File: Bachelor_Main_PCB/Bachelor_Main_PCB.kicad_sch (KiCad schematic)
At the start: 4 parts

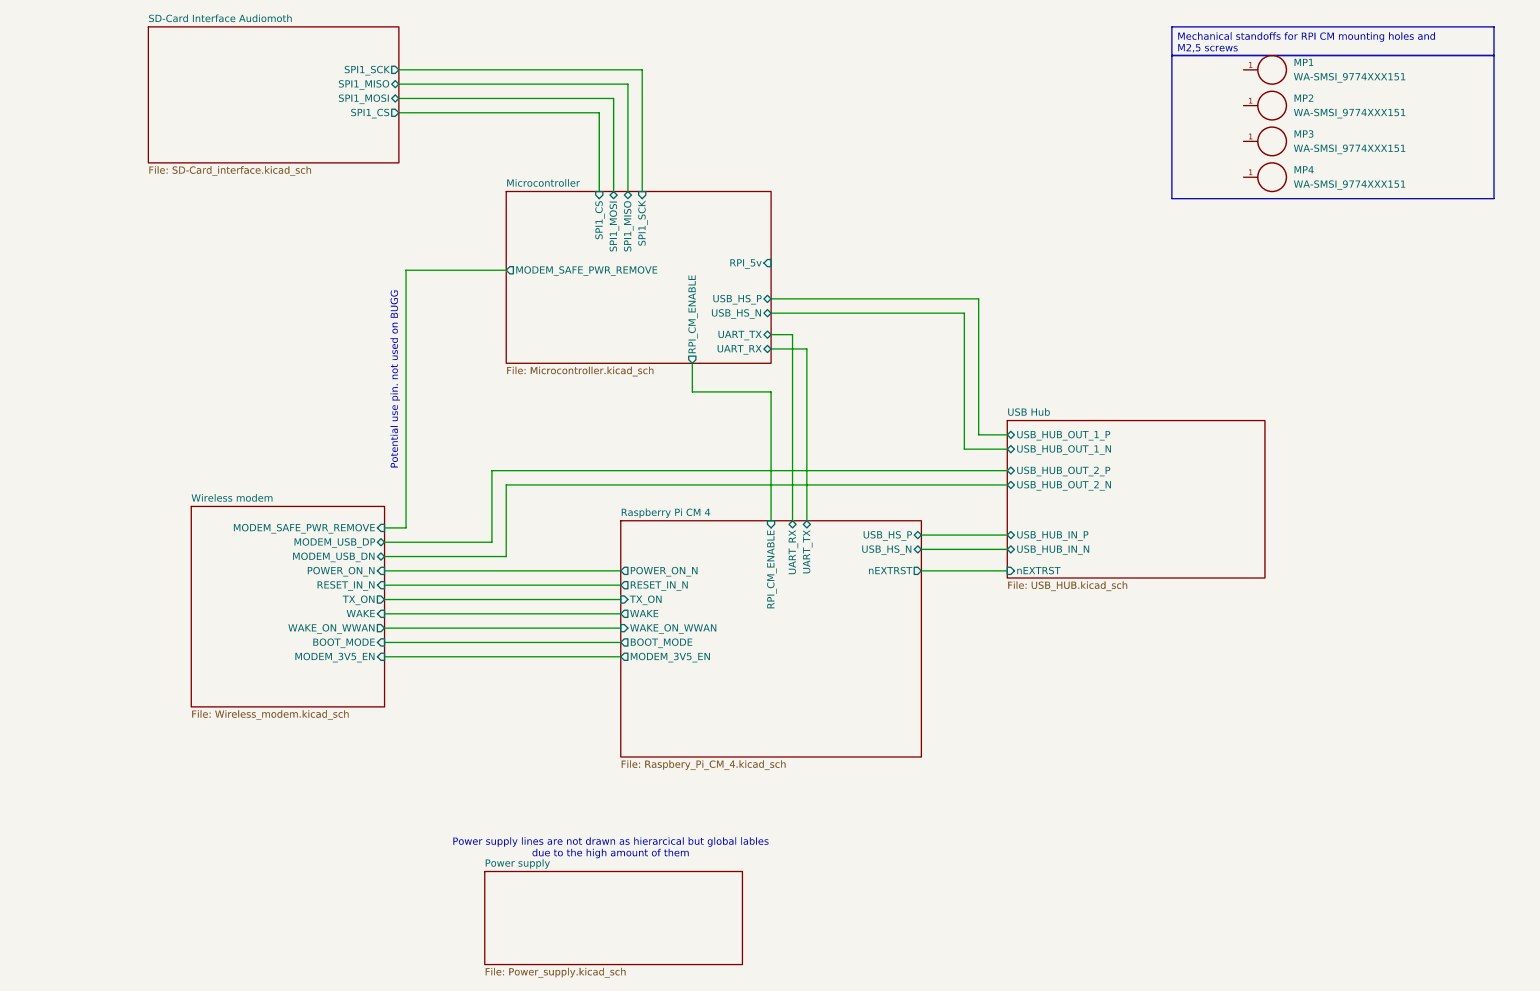
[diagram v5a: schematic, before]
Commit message: Add Vin sampling and route V_IN and V_IMON to MCU sheet
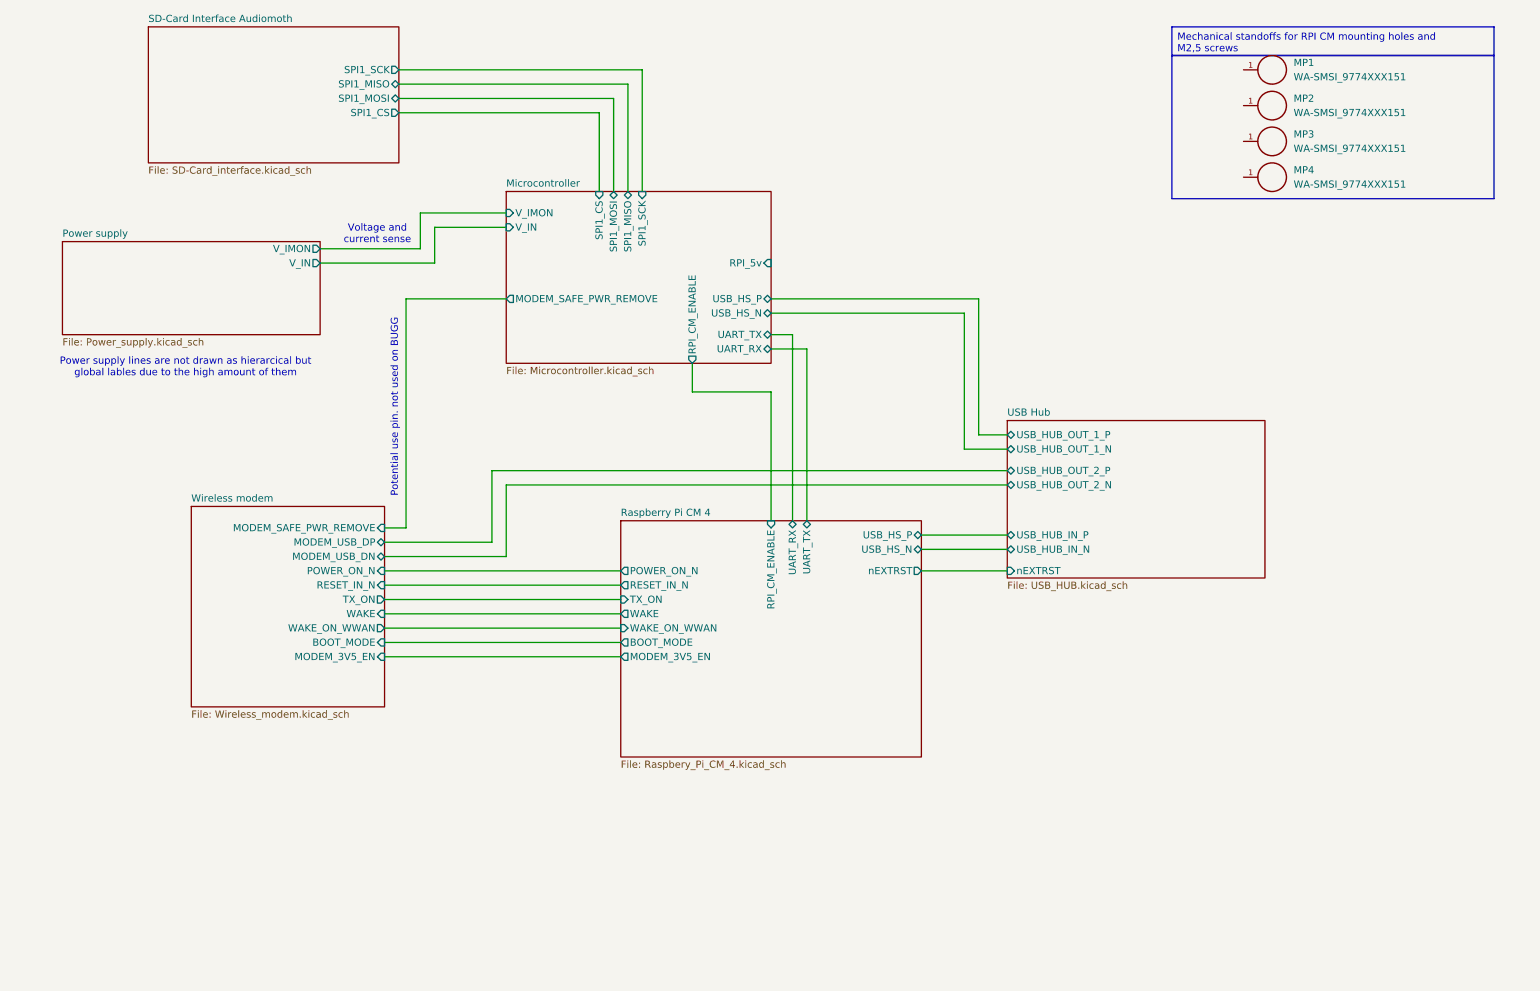
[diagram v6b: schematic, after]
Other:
- sheet Microcontroller ports: added V_IMON, V_IN; removed none
- sheet Power supply ports: added V_IMON, V_IN; removed none
- note added: "Voltage and current sense"
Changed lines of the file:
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@@
 	(generator_version "9.0")
 	(paper "A4")
-	(text "Power supply lines are not drawn as hierarcical but global lables\ndue to the high amount of them"
+	(text "Voltage and \ncurrent sense"
 		(exclude_from_sim no)
-		(at 120.142 163.576 0)
+		(at 78.74 54.61 0)
 		(effects
 			(font
@@
 		)
 	)
+	(text "Power supply lines are not drawn as hierarcical but \nglobal lables due to the high amount of them"
+		(exclude_from_sim no)
+		(at 44.704 78.232 0)
+		(effects
+			(font
+				(size 1.27 1.27)
+			)
+		)
+	)
 	(text "Potential use pin. not used on BUGG"
 		(exclude_from_sim no)
-		(at 81.788 80.518 90)
+		(at 81.788 85.344 90)
 		(effects
 			(font
@@
 	(wire
 		(pts
+			(xy 86.36 57.15) (xy 86.36 50.8)
+		)
+		(stroke
+			(width 0)
+			(type default)
+		)
+	)
+	(wire
+		(pts
 			(xy 120.65 30.48) (xy 82.55 30.48)
 		)
@@
 	(wire
 		(pts
-			(xy 83.82 60.96) (xy 101.6 60.96)
+			(xy 83.82 66.04) (xy 101.6 66.04)
 		)
 		(stroke
@@
 	(wire
 		(pts
+			(xy 101.6 53.34) (xy 88.9 53.34)
+		)
+		(stroke
+			(width 0)
+			(type default)
+		)
+	)
+	(wire
+		(pts
 			(xy 148.59 105.41) (xy 148.59 82.55)
 		)
@@
 	(wire
 		(pts
+			(xy 86.36 50.8) (xy 101.6 50.8)
+		)
+		(stroke
+			(width 0)
+			(type default)
+		)
+	)
+	(wire
+		(pts
+			(xy 88.9 59.69) (xy 68.58 59.69)
+		)
+		(stroke
+			(width 0)
+			(type default)
+		)
+	)
+	(wire
+		(pts
 			(xy 80.01 124.46) (xy 121.92 124.46)
 		)
@@
 	(wire
 		(pts
-			(xy 83.82 106.68) (xy 83.82 60.96)
+			(xy 83.82 106.68) (xy 83.82 66.04)
 		)
 		(stroke
@@
 	(wire
 		(pts
+			(xy 88.9 53.34) (xy 88.9 59.69)
+		)
+		(stroke
+			(width 0)
+			(type default)
+		)
+	)
+	(wire
+		(pts
 			(xy 134.62 82.55) (xy 134.62 77.47)
 		)
@@
 		(pts
 			(xy 80.01 119.38) (xy 121.92 119.38)
+		)
+		(stroke
+			(width 0)
+			(type default)
+		)
+	)
+	(wire
+		(pts
+			(xy 68.58 57.15) (xy 86.36 57.15)
 		)
 		(stroke
@@
 	)
 	(sheet
-		(at 97.79 167.64)
+		(at 22.86 55.88)
 		(size 45.72 16.51)
 		(exclude_from_sim no)
@@
 		)
 		(property "Sheetname" "Power supply"
-			(at 97.79 166.9284 0)
+			(at 22.86 55.1684 0)
 			(effects
 				(font
@@
 		)
 		(property "Sheetfile" "Power_supply.kicad_sch"
-			(at 97.79 184.7346 0)
+			(at 22.86 72.9746 0)
 			(effects
 				(font
@@
 				)
 				(justify left top)
+			)
+		)
+		(pin "V_IMON" output
+			(at 68.58 57.15 0)
+			(effects
+				(font
+					(size 1.27 1.27)
+				)
+				(justify right)
+			)
+		)
+		(pin "V_IN" output
+			(at 68.58 59.69 0)
+			(effects
+				(font
+					(size 1.27 1.27)
+				)
+				(justify right)
 			)
 		)
@@
 		)
 		(pin "MODEM_SAFE_PWR_REMOVE" output
-			(at 101.6 60.96 180)
+			(at 101.6 66.04 180)
 			(effects
 				(font
@@
 			)
 		)
+		(pin "V_IMON" input
+			(at 101.6 50.8 180)
+			(effects
+				(font
+					(size 1.27 1.27)
+				)
+				(justify left)
+			)
+		)
+		(pin "V_IN" input
+			(at 101.6 53.34 180)
+			(effects
+				(font
+					(size 1.27 1.27)
+				)
+				(justify left)
+			)
+		)

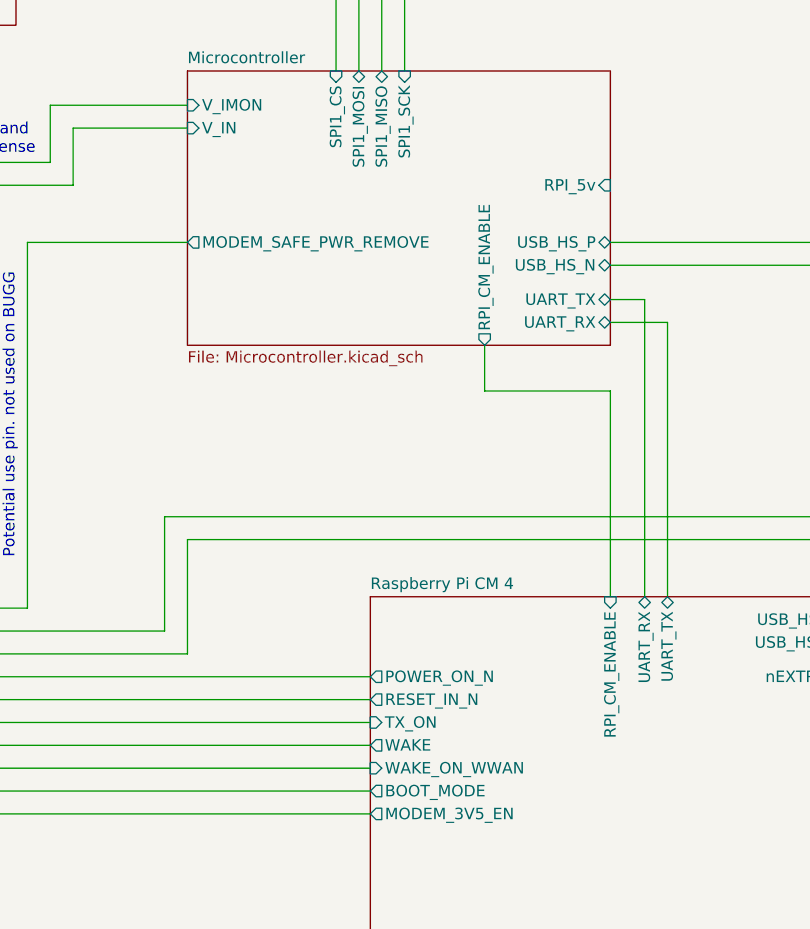
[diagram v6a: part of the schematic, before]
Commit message: Remove RPI CM power on mosfet. Replaced with EN pin to PSU
the pin is now routed instead to the LMR51450 converter ENABLE pin.
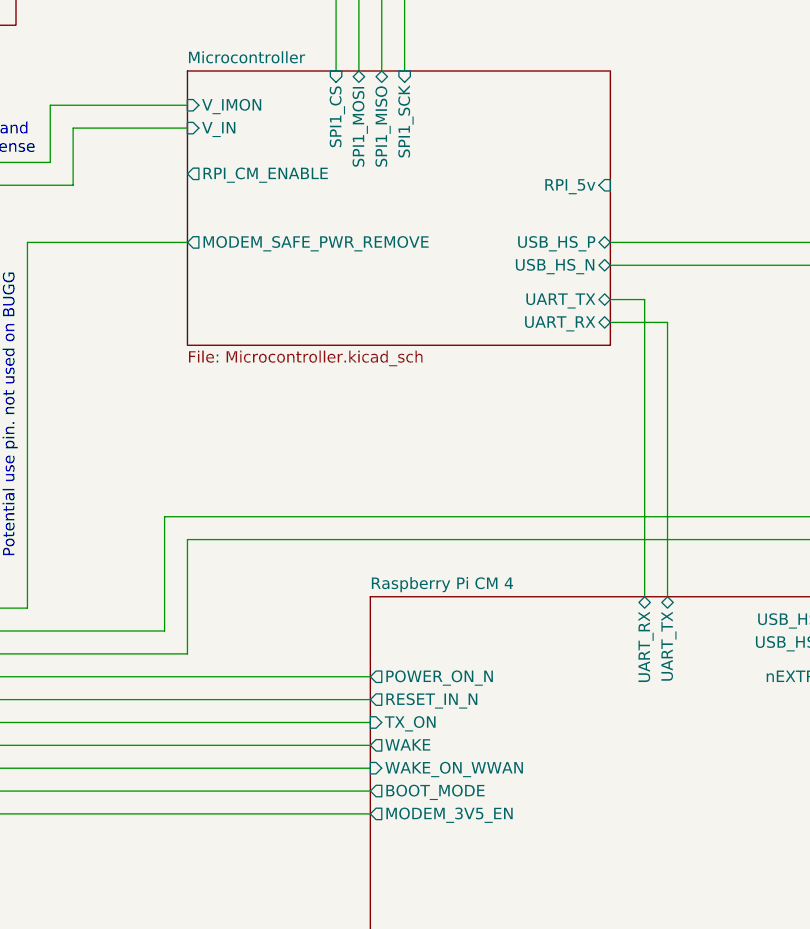
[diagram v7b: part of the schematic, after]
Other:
- sheet Raspberry Pi CM 4 ports: added none; removed RPI_CM_ENABLE
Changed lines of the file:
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@@
-	(wire
-		(pts
-			(xy 148.59 105.41) (xy 148.59 82.55)
-		)
-		(stroke
-			(width 0)
-			(type default)
-		)
-	)
 	(wire
 		(pts
@@
 	(wire
 		(pts
-			(xy 148.59 82.55) (xy 134.62 82.55)
-		)
-		(stroke
-			(width 0)
-			(type default)
-		)
-	)
-	(wire
-		(pts
 			(xy 88.9 53.34) (xy 88.9 59.69)
-		)
-		(stroke
-			(width 0)
-			(type default)
-		)
-	)
-	(wire
-		(pts
-			(xy 134.62 82.55) (xy 134.62 77.47)
 		)
 		(stroke
@@
 			)
 		)
-		(pin "RPI_CM_ENABLE" input
-			(at 148.59 105.41 90)
-			(effects
-				(font
-					(size 1.27 1.27)
-				)
-				(justify right)
-			)
-		)
 		(instances
 			(project "Bachelor_Main_PCB"
@@
 		)
 		(pin "RPI_CM_ENABLE" output
-			(at 134.62 77.47 270)
-			(effects
-				(font
+			(at 101.6 58.42 180)
+			(effects
+				(font

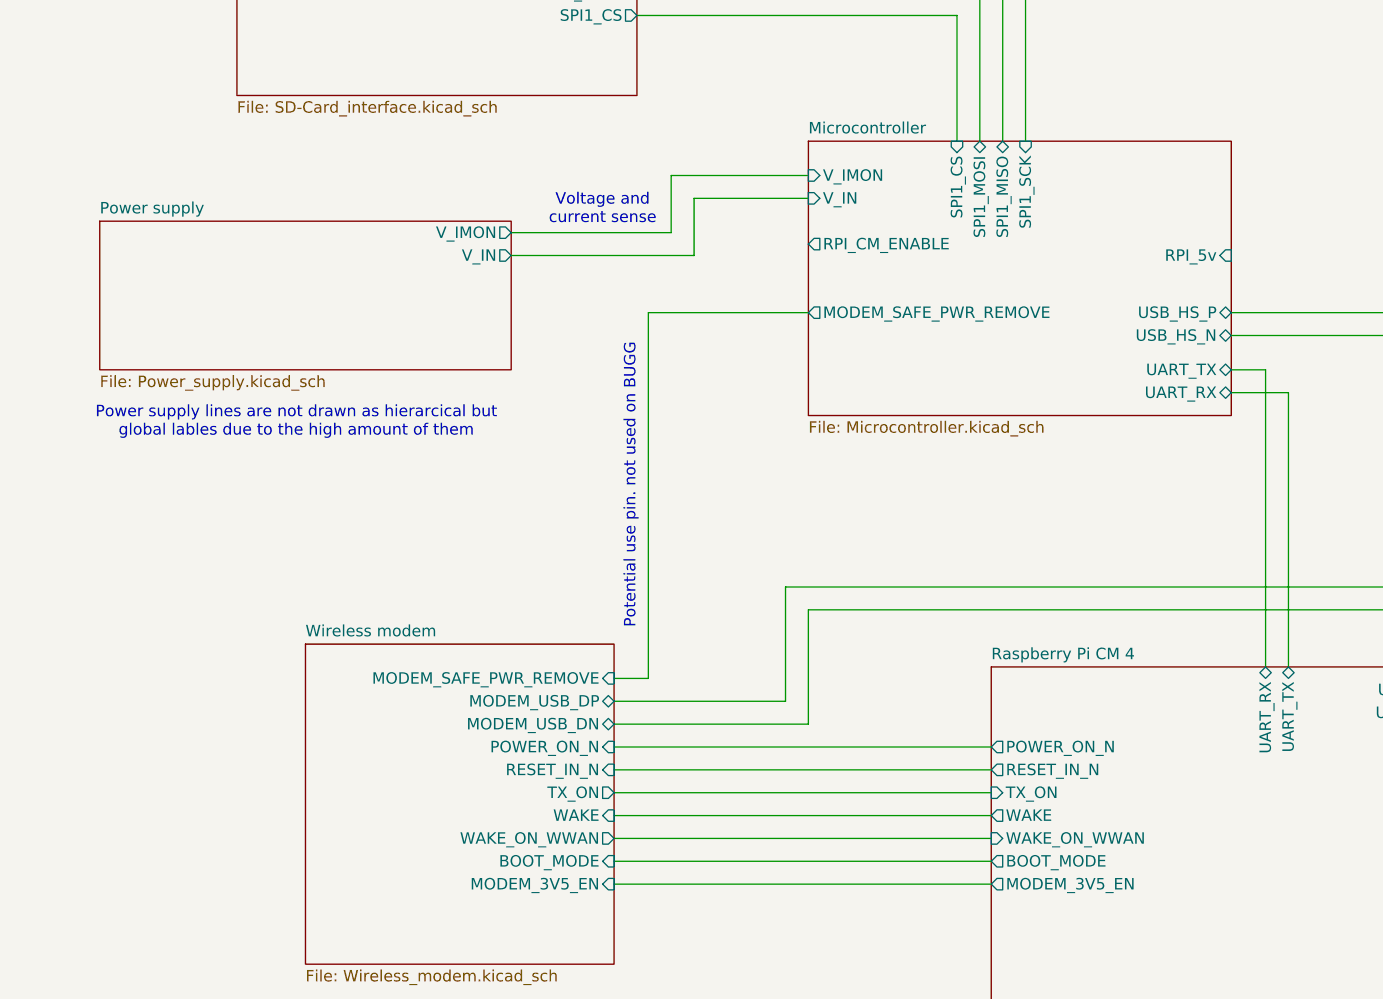
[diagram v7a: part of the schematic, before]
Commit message: Reinstated Mosfet RPI_CM_ENABLE controll
instead of enable pin on switch mode controller. this way the audiomoth can use the 5v supply with the capacitor multiplier.
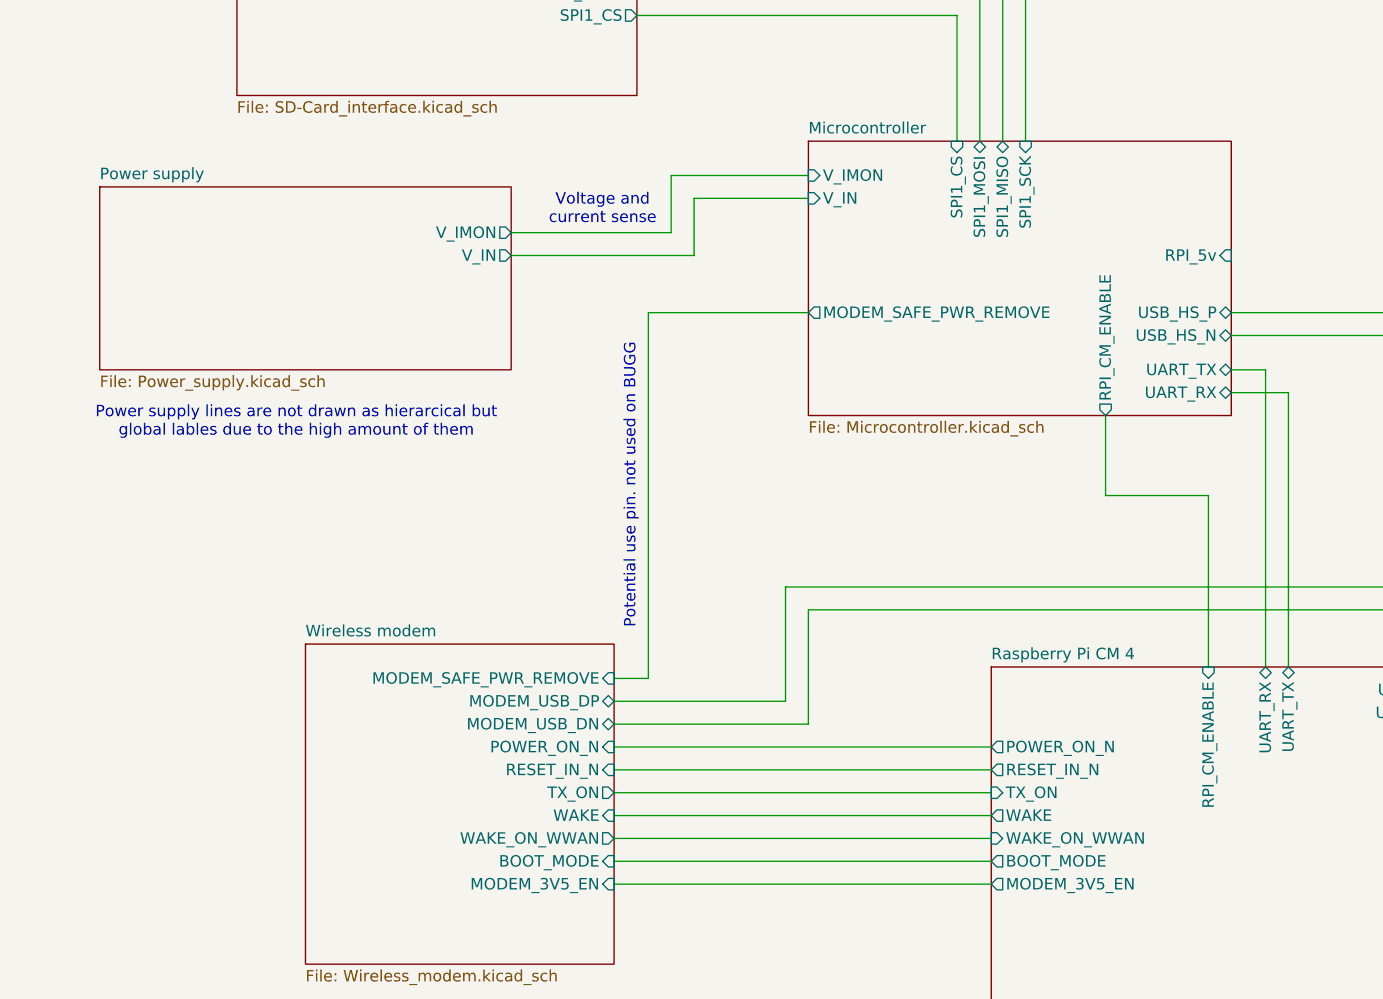
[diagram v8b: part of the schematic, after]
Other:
- sheet Raspberry Pi CM 4 ports: added RPI_CM_ENABLE; removed none
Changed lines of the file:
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@@
+	(wire
+		(pts
+			(xy 146.05 86.36) (xy 146.05 105.41)
+		)
+		(stroke
+			(width 0)
+			(type default)
+		)
+	)
 	(wire
 		(pts
@@
 	(wire
 		(pts
+			(xy 134.62 86.36) (xy 146.05 86.36)
+		)
+		(stroke
+			(width 0)
+			(type default)
+		)
+	)
+	(wire
+		(pts
 			(xy 125.73 46.99) (xy 125.73 25.4)
 		)
@@
 		(pts
 			(xy 99.06 96.52) (xy 99.06 109.22)
+		)
+		(stroke
+			(width 0)
+			(type default)
+		)
+	)
+	(wire
+		(pts
+			(xy 134.62 77.47) (xy 134.62 86.36)
 		)
 		(stroke
@@
 			)
 		)
+		(pin "RPI_CM_ENABLE" input
+			(at 146.05 105.41 90)
+			(effects
+				(font
+					(size 1.27 1.27)
+				)
+				(justify right)
+			)
+		)
 		(instances
 			(project "Bachelor_Main_PCB"
@@
 	)
 	(sheet
-		(at 22.86 55.88)
-		(size 45.72 16.51)
+		(at 22.86 52.07)
+		(size 45.72 20.32)
 		(exclude_from_sim no)
 		(in_bom yes)
@@
 		)
 		(property "Sheetname" "Power supply"
-			(at 22.86 55.1684 0)
+			(at 22.86 51.3584 0)
 			(effects
 				(font
@@
 		)
 		(pin "RPI_CM_ENABLE" output
-			(at 101.6 58.42 180)
-			(effects
-				(font
+			(at 134.62 77.47 270)
+			(effects
+				(font
